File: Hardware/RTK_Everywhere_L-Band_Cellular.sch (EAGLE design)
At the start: 294 parts, among them J3 MICRO-SD-PUSH-PUSH-EXT-PIN, J4 Vertical Qwiic Connector, J9 MAGJACK-POE, U1 ESP32-WROVER-IE, U10 POE_PSU-DP990X, U11 MCP6021T, U12 AP7361C-33, U13 MCP6021T, U14 BP2G1+_POWER_SPLITTER, U15 USB251XB_USB2514B, U16 SN74AVC4T774PW, U17 URB2405YMD, U2 CH340C, U3 XC6222B331MR-G, U4 U-BLOX_ZED-F9P, U5 U-BLOX_NEO-D9S-00B, U6 XC6222B331MR-G, U7 W5500, U8 LARA-R6001D, U9 74LVC4066D_QUAD_BILATERAL_SWI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, Y1 25MHz, Y2 24MHz

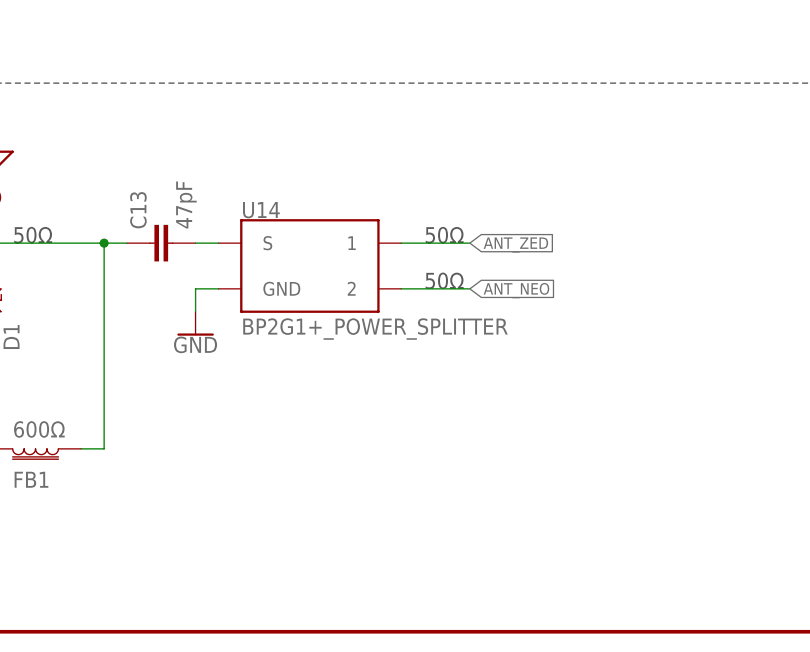
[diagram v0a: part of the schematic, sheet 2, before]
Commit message: Add no L-Band bypass. Update silk. Increase display cutout.
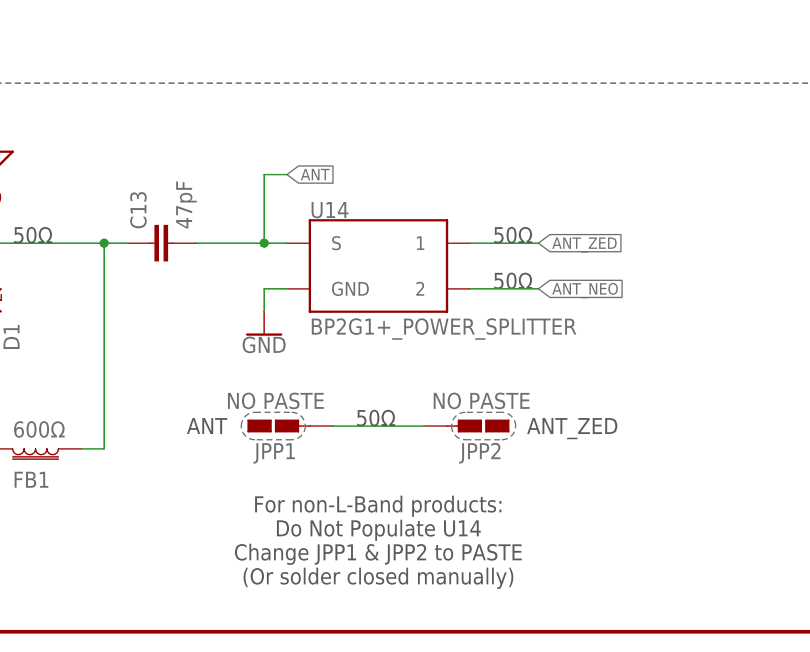
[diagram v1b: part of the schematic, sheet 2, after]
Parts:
- added JPP1, JPP2: NO PASTE, SparkFun-Jumpers:JUMPER-SMT_2_SOIC-PAD_NO-PASTE
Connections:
- net N$42 renamed ANT
- new net BYPASS: JPP1.1, JPP2.1
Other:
- note added: "ANT"
- note added: "ANT_ZED"
- note added: "For non-L-Band products: Do Not Populate U14 Change JPP1 & JPP2 to PASTE (Or solder closed manually)"
- note added: "RF Track Impedance: Coplanar Waveguide with Ground Calculations Ground is on layer 2. Prepreg thickness: 0.2mm. Er = 4.6 13.74 mil track with 8 mil gap = 50 Ohms https://saturnpcb.com/saturn-pcb-toolkit/"
- note added: "RTK Product Voltage IDs: Surveyor: Express: Reference Station: Facet: Facet L-Band: Express Plus: Everywhere:"
- note removed: "RF Track Impedance: Coplanar Waveguide with Ground Calculations Ground is on layer 2. Prepreg thickness: 0.2mm. Er = 4.6 12.5 mil track with 5 mil gap = 50 Ohms https://chemandy.com/calculators/coplanar-waveguide-with-ground-calculator.htm"
- note removed: "RTK Product Voltage IDs: Surveyor: Express: Reference Station: Facet: Facet L-Band: Express Plus: Control:"
- moved on the sheet: U14
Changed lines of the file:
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@@
 <part name="ESP5" library="SparkFun-Connectors" deviceset="TEST-POINT" device="POGO_PTH" value="TEST-POINTPOGO_PTH"/>
 <part name="GND49" library="SparkFun-PowerSymbols" deviceset="GND" device=""/>
+<part name="JPP1" library="SparkFun-Jumpers" deviceset="JUMPER-SMT_2_SOIC-PAD_NO-PASTE" device="" value="NO PASTE"/>
+<part name="JPP2" library="SparkFun-Jumpers" deviceset="JUMPER-SMT_2_SOIC-PAD_NO-PASTE" device="" value="NO PASTE"/>
 </parts>
 <sheets>
@@
 <text x="5.842" y="5.588" size="1.778" layer="97" font="vector">RF Track Impedance: Coplanar Waveguide with Ground Calculations
 Ground is on layer 2. Prepreg thickness: 0.2mm. Er = 4.6
-12.5 mil track with 5 mil gap = 50 Ohms
-https://chemandy.com/calculators/coplanar-waveguide-with-ground-calculator.htm</text>
+13.74 mil track with 8 mil gap = 50 Ohms
+https://saturnpcb.com/saturn-pcb-toolkit/</text>
 <text x="5.842" y="30.988" size="1.778" layer="97" font="vector" align="top-left">USB Track Impedance: Differential Pair
 https://saturnpcb.com/saturn-pcb-toolkit/
@@
 Facet L-Band:
 Express Plus:
-Control:</text>
+Everywhere:</text>
 <text x="176.022" y="28.448" size="1.778" layer="97" font="vector" align="top-left">
 Pin 35 floats at 0.18V approx.
@@
 <attribute name="NAME" x="188.468" y="265.43" size="1.778" layer="95" font="vector"/>
 </instance>
-<instance part="J8" gate="G$1" x="170.18" y="259.08" smashed="yes">
+<instance part="J8" gate="J1" x="170.18" y="259.08" smashed="yes">
 <attribute name="NAME" x="165.1" y="254" size="1.778" layer="95"/>
 <attribute name="VALUE" x="172.72" y="251.46" size="1.778" layer="96"/>
@@
 </segment>
 <segment>
-<pinref part="J8" gate="G$1" pin="GND"/>
+<pinref part="J8" gate="J1" pin="GND"/>
 <pinref part="GND59" gate="1" pin="GND"/>
 <wire x1="170.18" y1="254" x2="170.18" y2="251.46" width="0.1524" layer="91"/>
@@
 <net name="N$13" class="0">
 <segment>
-<pinref part="J8" gate="G$1" pin="SIGNAL"/>
+<pinref part="J8" gate="J1" pin="SIGNAL"/>
 <pinref part="ESP32_RF" gate="G$1" pin="SIGNAL"/>
 <wire x1="175.26" y1="259.08" x2="177.8" y2="259.08" width="0.1524" layer="91"/>
@@
 <wire x1="330.2" y1="88.9" x2="330.2" y2="157.48" width="0.1524" layer="97" style="longdash"/>
 <wire x1="330.2" y1="88.9" x2="431.8" y2="88.9" width="0.1524" layer="97" style="longdash"/>
-<text x="284.48" y="43.18" size="1.778" layer="97" font="vector">50Ω</text>
-<text x="284.48" y="38.1" size="1.778" layer="97" font="vector">50Ω</text>
+<text x="292.1" y="43.18" size="1.778" layer="97" font="vector">50Ω</text>
+<text x="292.1" y="38.1" size="1.778" layer="97" font="vector">50Ω</text>
 <text x="111.76" y="194.31" size="1.27" layer="97" font="vector" rot="R180" align="bottom-center">Close jumpers to
 enable pull-ups</text>
+<text x="276.86" y="22.86" size="1.778" layer="97" font="vector">50Ω</text>
+<text x="279.4" y="10.16" size="1.778" layer="97" font="vector" align="center">For non-L-Band products:
+Do Not Populate U14
+Change JPP1 &amp; JPP2 to PASTE
+(Or solder closed manually)</text>
+<text x="260.35" y="22.86" size="1.778" layer="97" font="vector" align="center">ANT</text>
+<text x="300.99" y="22.86" size="1.778" layer="97" font="vector" align="center">ANT_ZED</text>
 </plain>
 <instances>
@@
 <attribute name="VALUE" x="45.72" y="261.874" size="1.778" layer="96" font="vector" align="bottom-center"/>
 </instance>
-<instance part="U14" gate="U1" x="271.78" y="40.64" smashed="yes">
-<attribute name="NAME" x="264.16" y="45.974" size="1.778" layer="95" font="vector"/>
-<attribute name="VALUE" x="264.16" y="33.02" size="1.778" layer="96" font="vector"/>
+<instance part="U14" gate="U1" x="279.4" y="40.64" smashed="yes">
+<attribute name="NAME" x="271.78" y="45.974" size="1.778" layer="95" font="vector"/>
+<attribute name="VALUE" x="271.78" y="33.02" size="1.778" layer="96" font="vector"/>
 </instance>
-<instance part="GND87" gate="1" x="259.08" y="33.02" smashed="yes">
-<attribute name="VALUE" x="259.08" y="32.766" size="1.778" layer="96" align="top-center"/>
+<instance part="GND87" gate="1" x="266.7" y="33.02" smashed="yes">
+<attribute name="VALUE" x="266.7" y="32.766" size="1.778" layer="96" align="top-center"/>
 </instance>
 <instance part="SUPPLY16" gate="G$1" x="25.4" y="200.66" smashed="yes">
@@
 <attribute name="VALUE" x="121.92" y="198.374" size="1.778" layer="96" font="vector" align="bottom-center"/>
 </instance>
+<instance part="JPP1" gate="J1" x="269.24" y="22.86" smashed="yes" rot="R180">
+<attribute name="NAME" x="267.97" y="20.066" size="1.778" layer="95" font="vector" rot="R180" align="center"/>
+<attribute name="VALUE" x="267.97" y="25.654" size="1.778" layer="96" font="vector" rot="R180" align="center"/>
+</instance>
+<instance part="JPP2" gate="J1" x="289.56" y="22.86" smashed="yes" rot="MR180">
+<attribute name="NAME" x="290.83" y="20.066" size="1.778" layer="95" font="vector" rot="MR180" align="center"/>
+<attribute name="VALUE" x="290.83" y="25.654" size="1.778" layer="96" font="vector" rot="MR180" align="center"/>
+</instance>
 </instances>
 <busses>
@@
 <segment>
 <pinref part="U14" gate="U1" pin="GND"/>
-<wire x1="261.62" y1="38.1" x2="259.08" y2="38.1" width="0.1524" layer="91"/>
+<wire x1="269.24" y1="38.1" x2="266.7" y2="38.1" width="0.1524" layer="91"/>
 <pinref part="GND87" gate="1" pin="GND"/>
-<wire x1="259.08" y1="38.1" x2="259.08" y2="35.56" width="0.1524" layer="91"/>
+<wire x1="266.7" y1="38.1" x2="266.7" y2="35.56" width="0.1524" layer="91"/>
 </segment>
 <segment>
@@
 <segment>
 <pinref part="U14" gate="U1" pin="2"/>
-<wire x1="281.94" y1="38.1" x2="289.56" y2="38.1" width="0.1524" layer="91"/>
-<label x="289.56" y="38.1" size="1.27" layer="95" xref="yes"/>
+<wire x1="289.56" y1="38.1" x2="297.18" y2="38.1" width="0.1524" layer="91"/>
+<label x="297.18" y="38.1" size="1.27" layer="95" xref="yes"/>
 </segment>
 </net>
@@
 </segment>
 </net>
-<net name="N$42" class="0">
+<net name="ANT" class="0">
 <segment>
 <pinref part="U14" gate="U1" pin="S"/>
 <pinref part="C13" gate="G$1" pin="2"/>
-<wire x1="261.62" y1="43.18" x2="259.08" y2="43.18" width="0.1524" layer="91"/>
+<wire x1="269.24" y1="43.18" x2="266.7" y2="43.18" width="0.1524" layer="91"/>
+<wire x1="266.7" y1="43.18" x2="259.08" y2="43.18" width="0.1524" layer="91"/>
+<wire x1="266.7" y1="43.18" x2="266.7" y2="50.8" width="0.1524" layer="91"/>
+<junction x="266.7" y="43.18"/>
+<wire x1="266.7" y1="50.8" x2="269.24" y2="50.8" width="0.1524" layer="91"/>
+<label x="269.24" y="50.8" size="1.27" layer="95" xref="yes"/>
 </segment>
 </net>
@@
 <segment>
 <pinref part="U14" gate="U1" pin="1"/>
-<wire x1="281.94" y1="43.18" x2="289.56" y2="43.18" width="0.1524" layer="91"/>
-<label x="289.56" y="43.18" size="1.27" layer="95" xref="yes"/>
+<wire x1="289.56" y1="43.18" x2="297.18" y2="43.18" width="0.1524" layer="91"/>
+<label x="297.18" y="43.18" size="1.27" layer="95" xref="yes"/>
 </segment>
 </net>
@@
 </segment>
 </net>
+<net name="BYPASS" class="0">
+<segment>
+<pinref part="JPP1" gate="J1" pin="1"/>
+<pinref part="JPP2" gate="J1" pin="1"/>
+<wire x1="274.32" y1="22.86" x2="284.48" y2="22.86" width="0.1524" layer="91"/>
+</segment>
+</net>

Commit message: Update RF Bypass SOIC Pad jumpers
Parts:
- renumbered JPP1 to BYPASS1, JPP2 to BYPASS2
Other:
- note added: "For non-L-Band products: Do Not Populate U14 Change BYPASS1 & BYPASS2 to PASTE (Or solder closed manually)"
- note removed: "For non-L-Band products: Do Not Populate U14 Change JPP1 & JPP2 to PASTE (Or solder closed manually)"
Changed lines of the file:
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@@
 <part name="ESP5" library="SparkFun-Connectors" deviceset="TEST-POINT" device="POGO_PTH" value="TEST-POINTPOGO_PTH"/>
 <part name="GND49" library="SparkFun-PowerSymbols" deviceset="GND" device=""/>
-<part name="JPP1" library="SparkFun-Jumpers" deviceset="JUMPER-SMT_2_SOIC-PAD_NO-PASTE" device="" value="NO PASTE"/>
-<part name="JPP2" library="SparkFun-Jumpers" deviceset="JUMPER-SMT_2_SOIC-PAD_NO-PASTE" device="" value="NO PASTE"/>
+<part name="BYPASS1" library="SparkFun-Jumpers" deviceset="JUMPER-SMT_2_SOIC-PAD_NO-PASTE" device="" value="NO PASTE"/>
+<part name="BYPASS2" library="SparkFun-Jumpers" deviceset="JUMPER-SMT_2_SOIC-PAD_NO-PASTE" device="" value="NO PASTE"/>
 </parts>
 <sheets>
@@
 <text x="279.4" y="10.16" size="1.778" layer="97" font="vector" align="center">For non-L-Band products:
 Do Not Populate U14
-Change JPP1 &amp; JPP2 to PASTE
+Change BYPASS1 &amp; BYPASS2 to PASTE
 (Or solder closed manually)</text>
-<text x="260.35" y="22.86" size="1.778" layer="97" font="vector" align="center">ANT</text>
-<text x="300.99" y="22.86" size="1.778" layer="97" font="vector" align="center">ANT_ZED</text>
+<text x="262.89" y="22.86" size="1.778" layer="97" font="vector" align="center">ANT</text>
+<text x="298.45" y="22.86" size="1.778" layer="97" font="vector" align="center">ANT_ZED</text>
 </plain>
 <instances>
@@
 <attribute name="VALUE" x="121.92" y="198.374" size="1.778" layer="96" font="vector" align="bottom-center"/>
 </instance>
-<instance part="JPP1" gate="J1" x="269.24" y="22.86" smashed="yes" rot="R180">
-<attribute name="NAME" x="267.97" y="20.066" size="1.778" layer="95" font="vector" rot="R180" align="center"/>
-<attribute name="VALUE" x="267.97" y="25.654" size="1.778" layer="96" font="vector" rot="R180" align="center"/>
-</instance>
-<instance part="JPP2" gate="J1" x="289.56" y="22.86" smashed="yes" rot="MR180">
-<attribute name="NAME" x="290.83" y="20.066" size="1.778" layer="95" font="vector" rot="MR180" align="center"/>
-<attribute name="VALUE" x="290.83" y="25.654" size="1.778" layer="96" font="vector" rot="MR180" align="center"/>
+<instance part="BYPASS1" gate="J1" x="269.24" y="22.86" smashed="yes" rot="R180">
+<attribute name="NAME" x="269.24" y="20.066" size="1.778" layer="95" font="vector" rot="R180" align="center"/>
+<attribute name="VALUE" x="269.24" y="25.654" size="1.778" layer="96" font="vector" rot="R180" align="center"/>
+</instance>
+<instance part="BYPASS2" gate="J1" x="289.56" y="22.86" smashed="yes" rot="MR180">
+<attribute name="NAME" x="289.56" y="20.066" size="1.778" layer="95" font="vector" rot="MR180" align="center"/>
+<attribute name="VALUE" x="289.56" y="25.654" size="1.778" layer="96" font="vector" rot="MR180" align="center"/>
 </instance>
 </instances>
@@
 <net name="BYPASS" class="0">
 <segment>
-<pinref part="JPP1" gate="J1" pin="1"/>
-<pinref part="JPP2" gate="J1" pin="1"/>
+<pinref part="BYPASS1" gate="J1" pin="1"/>
+<pinref part="BYPASS2" gate="J1" pin="1"/>
 <wire x1="274.32" y1="22.86" x2="284.48" y2="22.86" width="0.1524" layer="91"/>
 </segment>

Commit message: Add V10 PCB files
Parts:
- removed ESP5: TEST-POINTPOGO_PTH, SparkFun-Connectors:TEST-POINTPOGO_PTH
- removed JP1, JP2: JUMPER-SMT_2_NO_SILK, SparkFun-Jumpers:JUMPER-SMT_2_NO_SILK
- removed Q3, Q4: (no value), SparkFun-DiscreteSemi:TRANS_NPN_DUAL-MBT3904DW1T1
- removed R69: 10k, SparkFun-Resistors:10KOHM-0603-1/10W-1%
- added D15, D16, D17, D18, D19, D20: PESD0402-0402, SparkFun-DiscreteSemi:PESD0402-0402
- added LARA_ON, RXD, TXD, VCCIO: TEST-POINTPOGO_PTH, SparkFun-Connectors:TEST-POINTPOGO_PTH
- added Q5, Q6: 310mA/60V/1.6Ω, SparkFun-DiscreteSemi:MOSFET-NCH-2N7002PW
- added R50, R51, R52: 100k, SparkFun-Resistors:100KOHM-0603-1/10W-1%
- added SPWR, TPWR: JUMPER-SMT_3_1-NC_TRACE_SILK, SparkFun-Jumpers:JUMPER-SMT_3_1-NC_TRACE_SILK
- added U18: 74HC1G04, SparkFun-IC-Logic:74HC1G04
- added USB251SCL, USB251SDA: JUMPER-SMT_2_NO_SILK, SparkFun-Jumpers:JUMPER-SMT_2_NO_SILK
- FRAME2: DESIGNER Paul Clark -> (none); REV V01 -> (none)
- R44: value 10k -> 100k; device SparkFun-Resistors:10KOHM-0603-1/10W-1% -> SparkFun-Resistors:100KOHM-0603-1/10W-1%
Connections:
- net ESP26/LARA_ON renamed ESP26/LARA_PWR_ON
- net ESP5 renamed ESP5/LARA_ON
- removed net N$37: ESP5.1, U9.3Z
- removed net N$57: JP1.2, U15.SDA
- removed net N$58: JP2.2, U15.SCL/CFG0
- removed net N$59: Q4G1.C, Q4G2.B, R69.1
- removed net N$60: Q3G1.B, R68.2
- new net LARA_ON: LARA_ON.1, U16.B4, U9.3Z
- new net N$22: R50.1, SPWR.3
- new net N$26: SPWR.2, U3.EN
- new net N$31: R51.1, TPWR.3
- new net N$39: TPWR.2, U12.EN
- new net N$42: Q6.G, R68.2
- new net USB251SCL: R52.2, U15.SCL/CFG0, USB251SCL.2
- new net USB251SDA: R44.2, U15.SDA, USB251SDA.2
- net 3.3V_SW2: now also U18G2.P$V+; no longer R44.2, R69.2
- net 5V: now also R50.2, R51.2
- net ESP13/LARA_TXDI: now also TXD.1
- net ESP14/LARA_RXDO: now also RXD.1
- net ESP21/SDA: now also D15.1, USB251SDA.1; no longer JP1.1
- net ESP22/SCL: now also D16.1, USB251SCL.1; no longer JP2.1
- net ESP25/TP: now also D20.1
- net GND: now also D15.2, D16.2, D17.2, D18.2, D19.2, D20.2, Q5.S, Q6.S, R44.1, R52.1, U18G2.P$V-; no longer Q3G1.E, Q3G2.E, Q4G1.E, Q4G2.E
- net GNSS_!RESET!: now also U18G1.A; no longer R68.1
- net LARA_!RESET!: now also Q6.D; no longer Q3G2.C
- net LARA_PWR_ON: now also Q5.D; no longer Q4G2.C
- net N$16: now also R68.1, U18G1.Y; no longer Q3G1.C, Q3G2.B, R44.1
- net N$65: now also Q5.G; no longer Q4G1.B
- net PWREN: now also SPWR.1, TPWR.1; no longer U12.EN, U3.EN
- net VCCIO: now also VCCIO.1
- net ZED_EXTINT: now also D19.1
- net ZED_RX2: now also D17.1
- net ZED_TX2: now also D18.1
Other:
- note added: "v10"
- note removed: "Pin 35 floats at 0.18V approx. 3.3 / 13.3 = 0.82V (0.74 - 0.90) 10 / 30 = 1.1V (0.99 - 1.21) 10 / 20 = 1.65V (1.49 - 1.82) 20 / 30 = 2.2V (1.98 - 2.42) 10 / 13.3 = 2.48V (2.23 - 2.73) 10 / 11 = 3.00V (2.70 - 3.30)"
- note removed: "RTK Product Voltage IDs: Surveyor: Express: Reference Station: Facet: Facet L-Band: Express Plus: Everywhere:"
- note removed: "v01"
- moved on the sheet: C10, C52, C55, C60, C61, C63, C64, C65, C66, C67, C68, C8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
